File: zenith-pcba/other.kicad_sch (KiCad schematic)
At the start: 1 part, among them U1 XC7A50T-CSG325

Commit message: feat(pcba): migrate to kintex fpga
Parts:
- removed U1: XC7A50T-CSG325, Package_BGA:Xilinx_CSG325, symbol FPGA_Xilinx_Artix7:XC7A50T-CSG325
- added U1: XC7K70T-FBG676, easyeda2kicad:FBGA-676_L27.0-W27.0-R26-C26-P1.00-BL, symbol FPGA_Xilinx_Kintex7:XC7K70T-FBG676

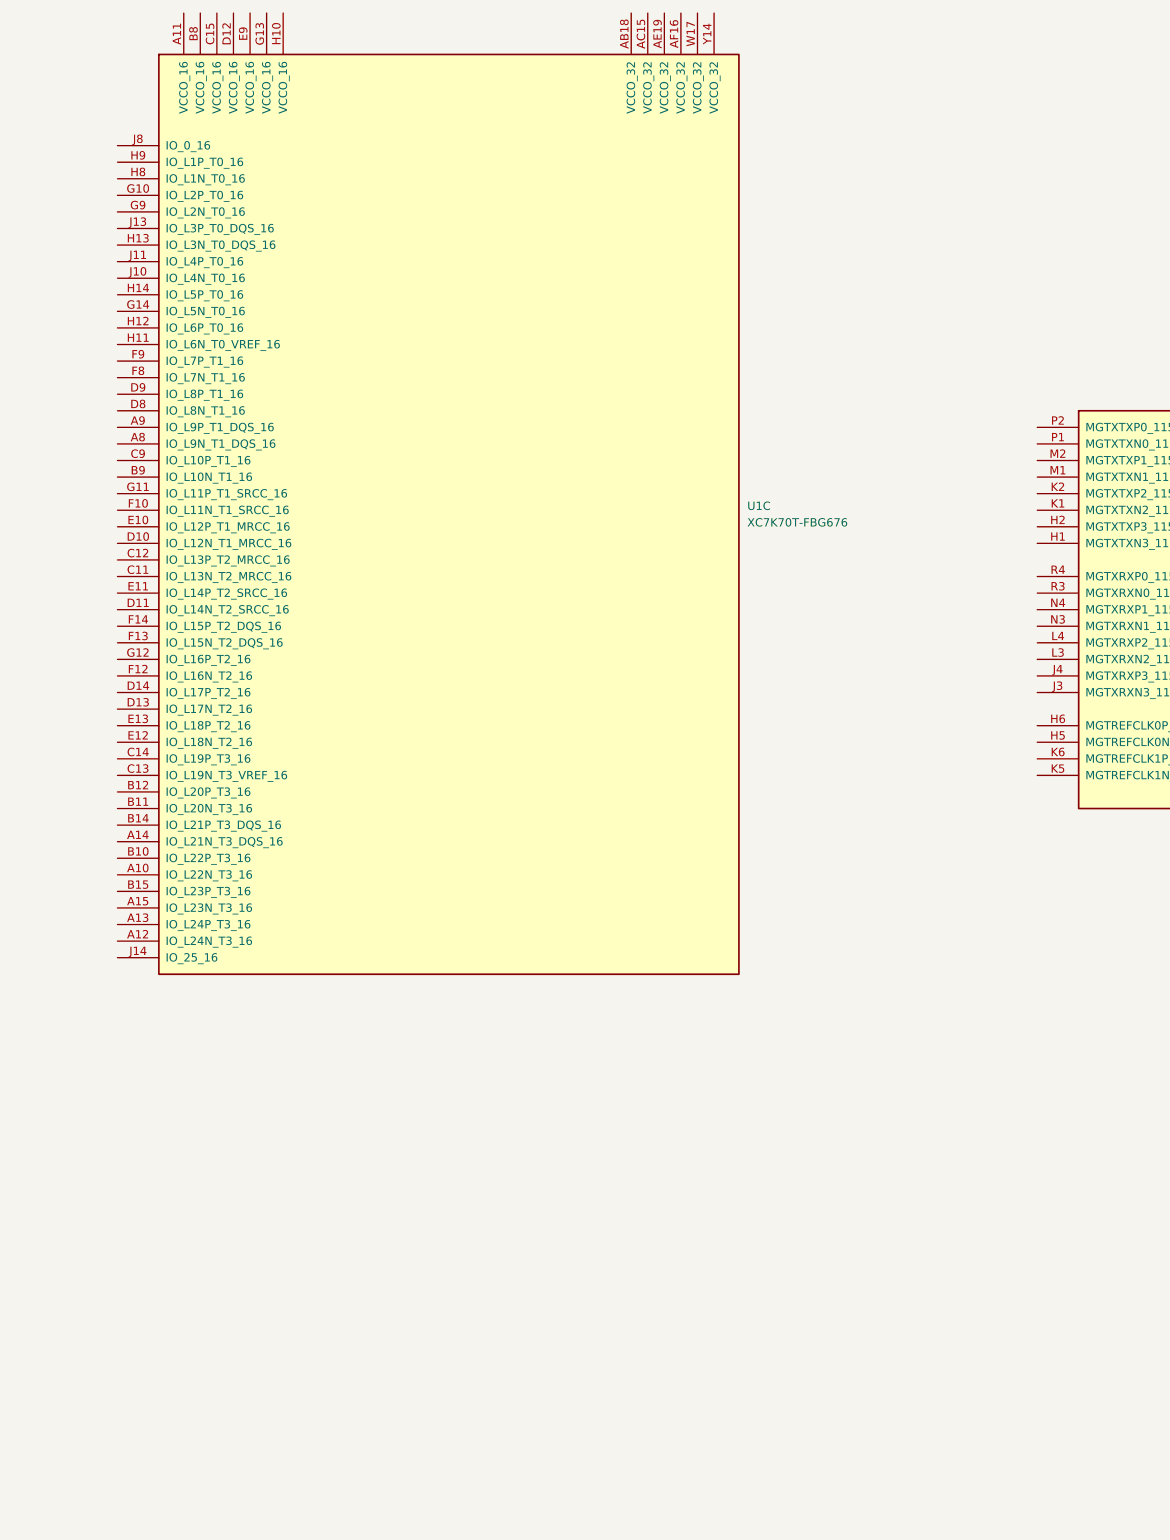
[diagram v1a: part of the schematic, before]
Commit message: feat(pcba): pcb edge cuts
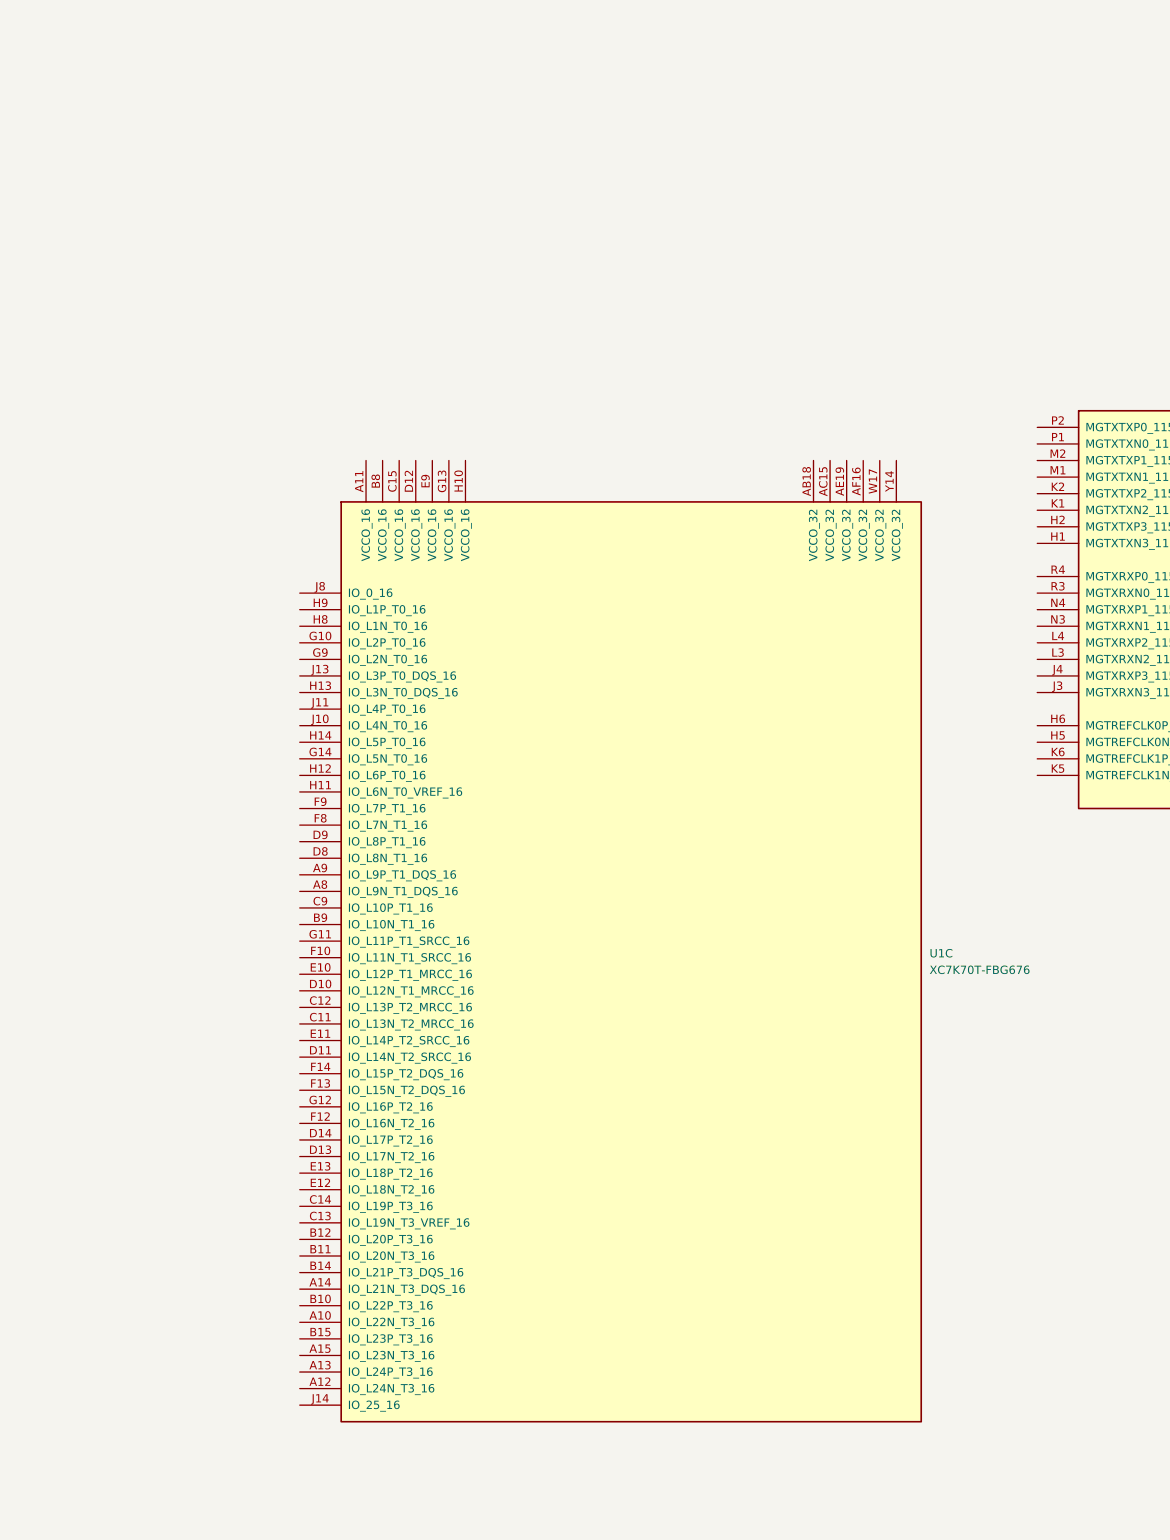
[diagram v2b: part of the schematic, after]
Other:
- moved on the sheet: U1C
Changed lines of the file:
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@@
 	(symbol
 		(lib_id "FPGA_Xilinx_Kintex7:XC7K70T-FBG676")
-		(at 303.53 -40.64 0)
+		(at 331.47 27.94 0)
 		(unit 3)
 		(body_style 1)
@@
 		(fields_autoplaced yes)
 		(property "Reference" "U1"
-			(at 349.25 -38.7351 0)
+			(at 377.19 29.8449 0)
 			(show_name no)
 			(do_not_autoplace no)
@@
 		)
 		(property "Value" "XC7K70T-FBG676"
-			(at 349.25 -36.1951 0)
+			(at 377.19 32.3849 0)
 			(show_name no)
 			(do_not_autoplace no)
@@
 		)
 		(property "Footprint" "easyeda2kicad:FBGA-676_L27.0-W27.0-R26-C26-P1.00-BL"
-			(at 303.53 -40.64 0)
+			(at 331.47 27.94 0)
 			(hide yes)
 			(show_name no)
@@
 		)
 		(property "Datasheet" ""
-			(at 303.53 -40.64 0)
+			(at 331.47 27.94 0)
 			(show_name no)
 			(do_not_autoplace no)
@@
 		)
 		(property "Description" "Kintex 7 T 70 XC7K70T-FBG676"
-			(at 303.53 -40.64 0)
+			(at 331.47 27.94 0)
 			(hide yes)
 			(show_name no)
